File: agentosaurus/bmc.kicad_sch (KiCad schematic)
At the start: 14 parts, among them J1 USB-C, U1 ESP32-S3-WROOM-1, U2 USBLC6-2SC6, U3 SN74LV4052ADR, U4 TS3USB221 Mux1, U5 TS3USB221 Mux2, U6 TPS22918 Slot1, U7 TPS22918 Slot2, U8 TPS22918 Slot3, U9 TPS22918 Slot4

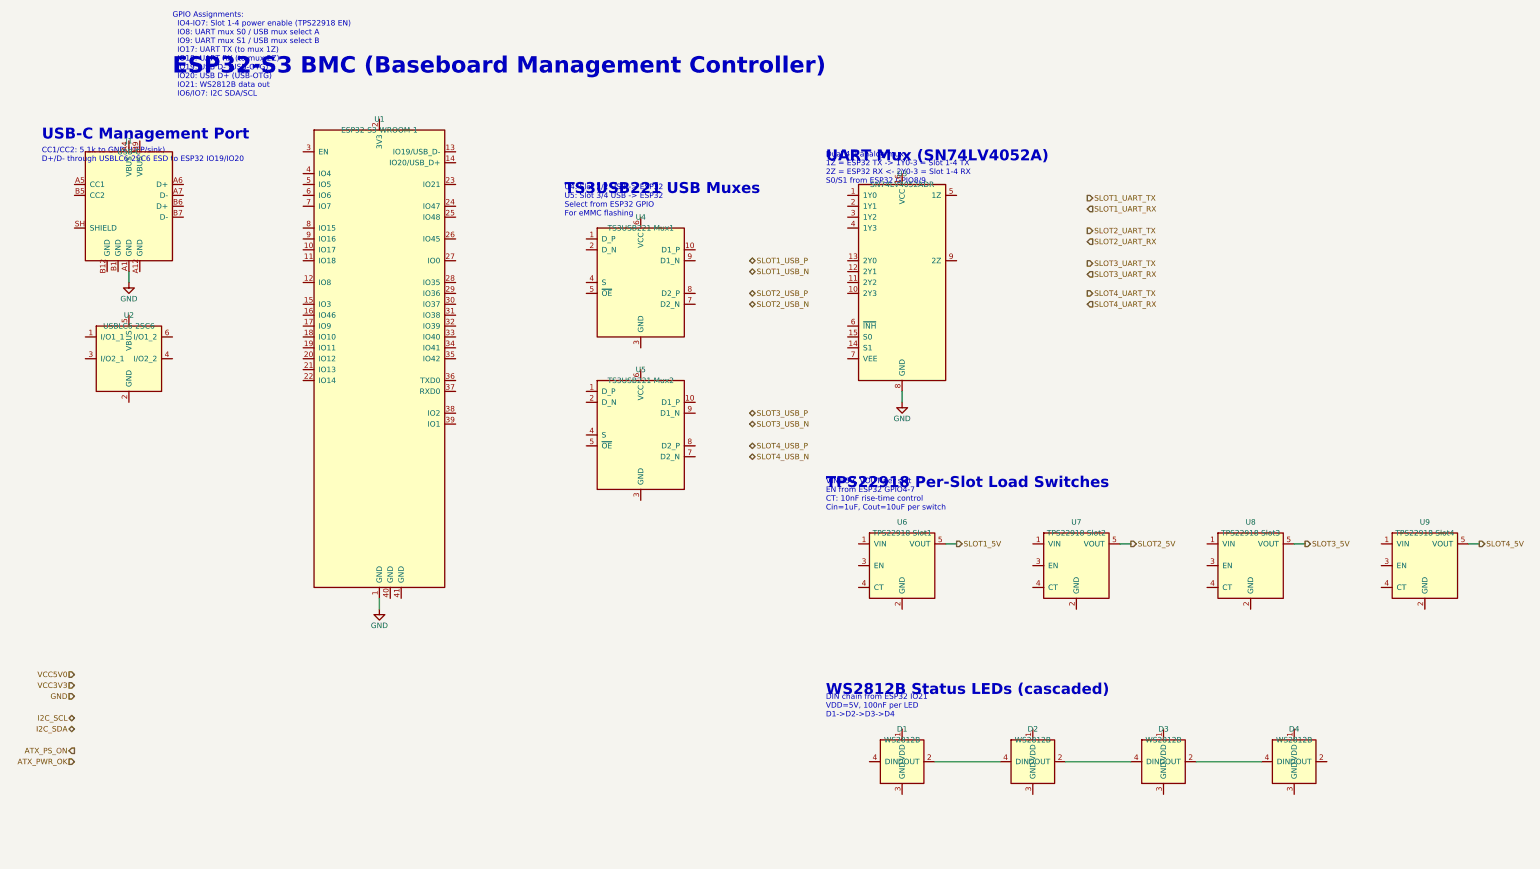
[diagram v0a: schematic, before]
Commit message: Add passive components to all schematic sheets
- power.kicad_sch: Fix D1 catch diode rotation (cathode→SW), remove
  incorrect COMP-to-output wire, add all TPS54360 application circuit
  passives (CIN1/2, CBOOT, L1, COUT1-3, R_EN1/2, R_RT, R_FB1/2,
  R_COMP, C_COMP) and AMS1117 caps (CIN_LDO, COUT_LDO)
- bmc.kicad_sch: Add USB-C CC pull-downs (R1/R2 5.1k), ESP32 reset
  circuit (R3 10k + C9 1uF), decoupling caps for ESP32 (C10/C11),
  UART mux (C12), USB mux (C13/C14), WS2812B (C15-C18), I2C
  pull-ups (R4/R5 4.7k)
- cm4-slot.kicad_sch: Add magnetics center-tap decoupling (C1-C4
  100nF) and power rail decoupling (C5-C8)
- ethernet-switch.kicad_sch: Add crystal load caps (C1/C2 22pF),
  3.3V decoupling (C3-C10), 1.0V core decoupling (C11-C16),
  Slot 2 Ethernet wiring to RTL8367S
- mechanical.kicad_sch: Add PCB stackup, impedance control, and
  via specifications

https://claude.ai/code/session_01UhhXLgEHsAy83XEALyNrDb
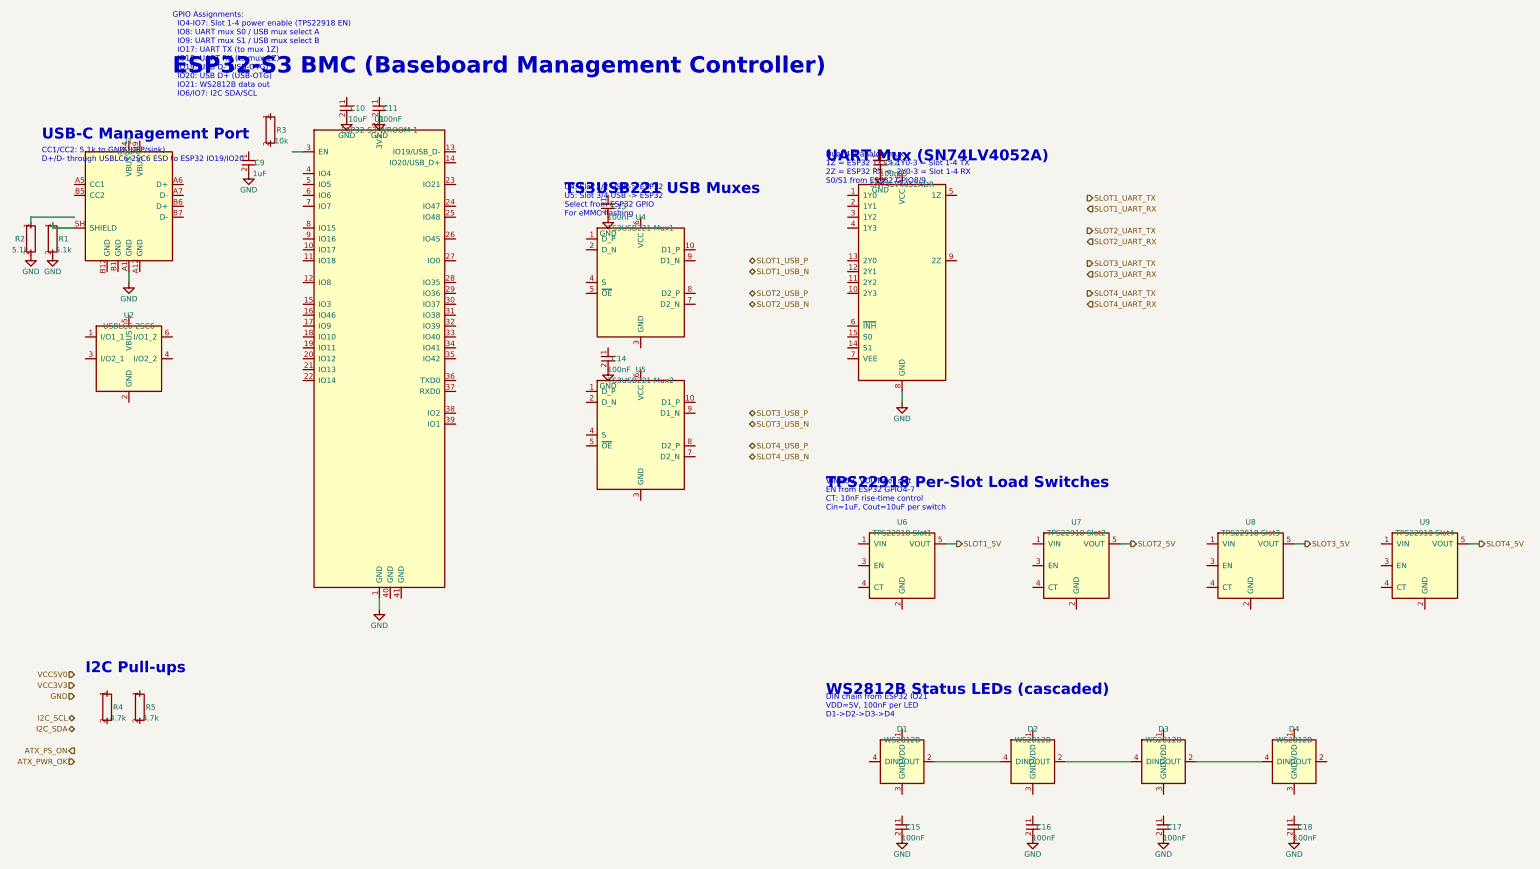
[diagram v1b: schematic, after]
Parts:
- added C10: 10uF, Capacitor_SMD:C_0805_2012Metric, symbol Device:C
- added C11, C12, C13, C14, C15, C16, C17, C18: 100nF, Capacitor_SMD:C_0402_1005Metric, symbol Device:C
- added C9: 1uF, Capacitor_SMD:C_0402_1005Metric, symbol Device:C
- added R1, R2: 5.1k, Resistor_SMD:R_0402_1005Metric, symbol Device:R
- added R3: 10k, Resistor_SMD:R_0402_1005Metric, symbol Device:R
- added R4, R5: 4.7k, Resistor_SMD:R_0402_1005Metric, symbol Device:R
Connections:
- net GND: now also U1.2 (3V3), C10.2, C11.2, C12.2, C13.2, C14.2, C15.2, C16.2, C17.2, C18.2, C9.2, R1.2, R2.2
- net at J1.SH (SHIELD): now also R1.1
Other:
- note added: "I2C Pull-ups"
